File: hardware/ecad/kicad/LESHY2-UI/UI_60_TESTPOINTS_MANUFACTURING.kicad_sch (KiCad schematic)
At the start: 0 parts

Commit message: complete exact H2.2.10 UI test points
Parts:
- added TP1: TP_S3_RUN, TestPoint:TestPoint_Pad_D1.0mm, symbol Leshy2:UI60_TP_S3_RUN
- added TP10: TP_SLOW_IO_RESET_N, TestPoint:TestPoint_Pad_D1.0mm, symbol Leshy2:UI60_TP_SLOW_IO_RESET_N
- added TP11: TP_LCD_BACKLIGHT_FAULT_N, TestPoint:TestPoint_Pad_D1.0mm, symbol Leshy2:UI60_TP_LCD_BACKLIGHT_FAULT_N
- added TP2: TP_C5_RUN, TestPoint:TestPoint_Pad_D1.0mm, symbol Leshy2:UI60_TP_C5_RUN
- added TP3: TP_UI_TEMP, TestPoint:TestPoint_Pad_D1.0mm, symbol Leshy2:UI60_TP_UI_TEMP
- added TP4: TP_IR_TX_SAFE, TestPoint:TestPoint_Pad_D1.0mm, symbol Leshy2:UI60_TP_IR_TX_SAFE
- added TP5: TP_EV_N0, TestPoint:TestPoint_Pad_D1.0mm, symbol Leshy2:UI60_TP_EV_N0
- added TP6: TP_EV_N1, TestPoint:TestPoint_Pad_D1.0mm, symbol Leshy2:UI60_TP_EV_N1
- added TP7: TP_EV_N7, TestPoint:TestPoint_Pad_D1.0mm, symbol Leshy2:UI60_TP_EV_N7
- added TP8: TP_C5_SERVICE_VBUS_SENSE, TestPoint:TestPoint_Pad_D1.0mm, symbol Leshy2:UI60_TP_C5_SERVICE_VBUS_SENSE
- added TP9: TP_C5_GPIO27_FIXED_HIGH, TestPoint:TestPoint_Pad_D1.0mm, symbol Leshy2:UI60_TP_C5_GPIO27_FIXED_HIGH
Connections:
- new net C5_GPIO27_FIXED_HIGH: TP9.1 (TEST)
- new net C5_RESET_N: TP2.1 (TEST)
- new net C5_SERVICE_VBUS_SENSE_ONLY: TP8.1 (TEST)
- new net EV_N0_S3: TP5.1 (TEST)
- new net EV_N1_C5: TP6.1 (TEST)
- new net EV_N7_IR: TP7.1 (TEST)
- new net IR_TX_CARRIER_SAFE: TP4.1 (TEST)
- new net LCD_BACKLIGHT_FAULT_N: TP11.1 (TEST)
- new net S3_RESET_N: TP1.1 (TEST)
- new net SLOW_IO_RESET_N: TP10.1 (TEST)
- new net UI_ZONE_TEMP_ADC: TP3.1 (TEST)
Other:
- title: (none) -> Leshy2 — exact UI manufacturing and diagnostic test pads

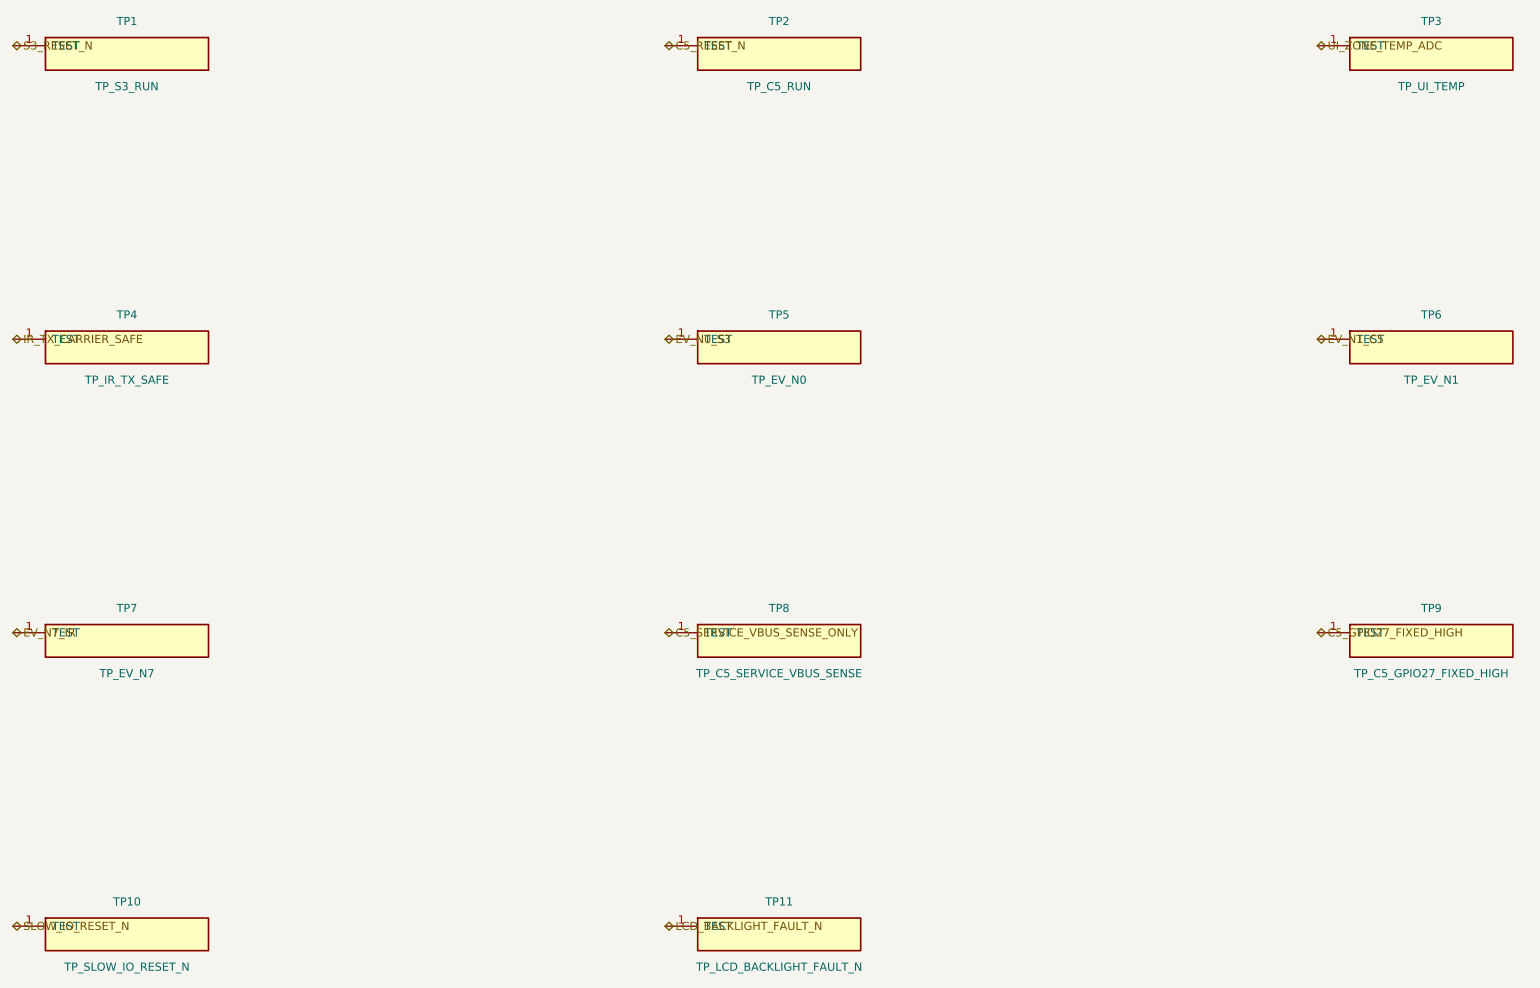
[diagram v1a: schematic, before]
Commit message: complete H2 schematic review package
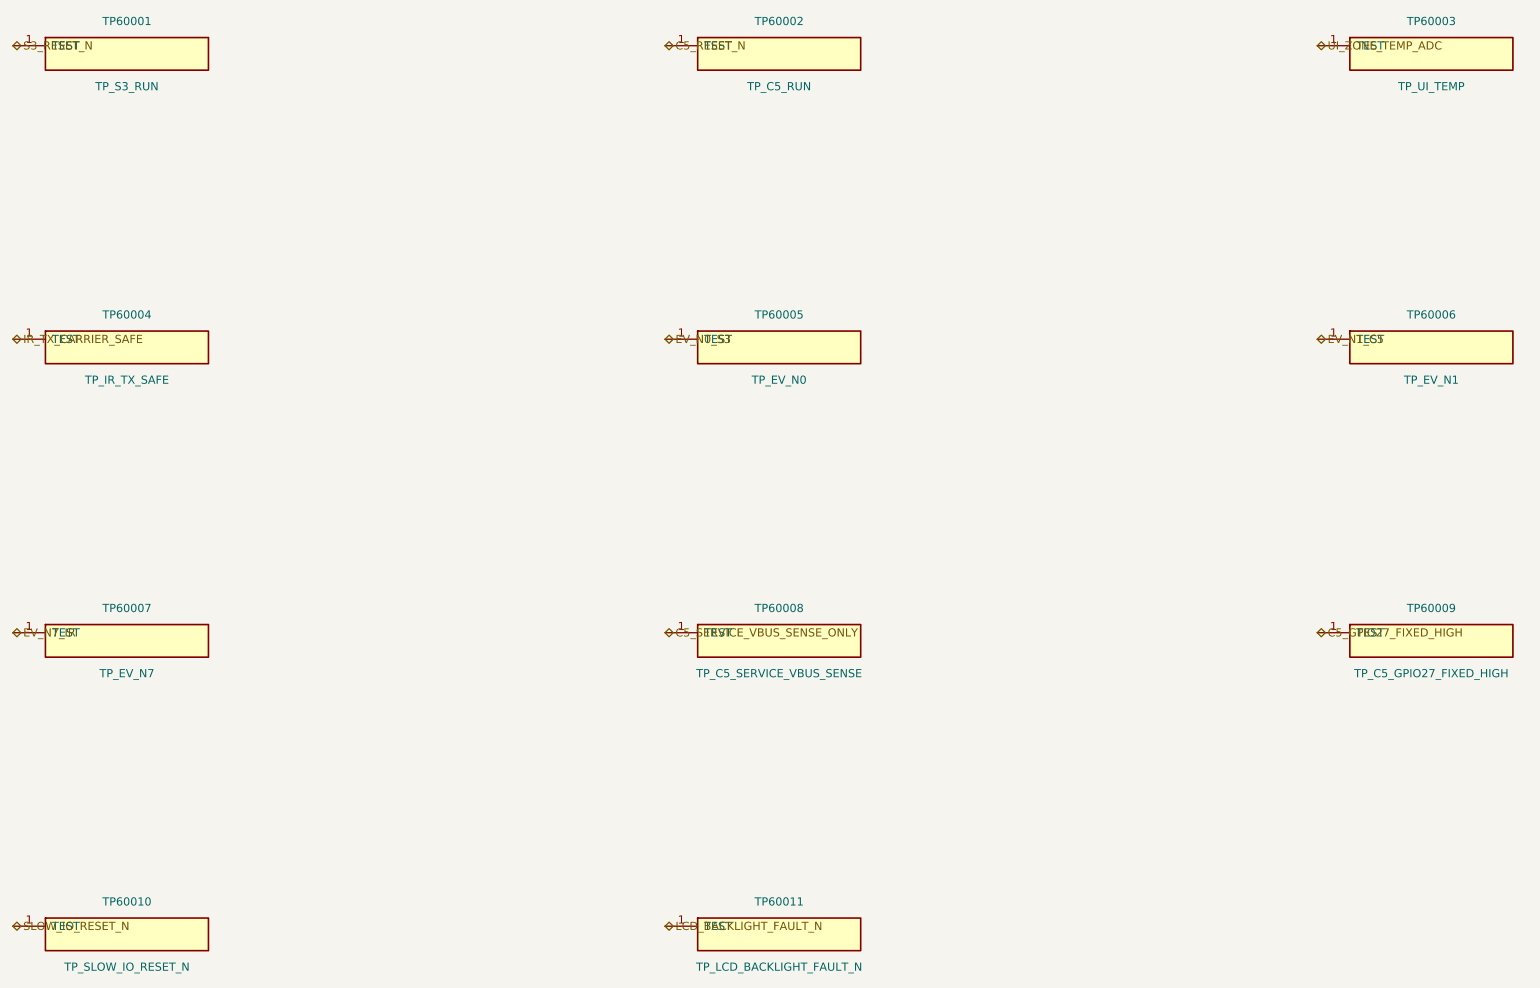
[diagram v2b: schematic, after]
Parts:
- renumbered TP1 to TP60001, TP2 to TP60002, TP3 to TP60003, TP4 to TP60004, TP5 to TP60005, TP6 to TP60006, TP7 to TP60007, TP8 to TP60008, TP9 to TP60009, TP10 to TP60010, TP11 to TP60011
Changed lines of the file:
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@@
 		(on_board yes)
 		(dnp no)
-		(property "Reference" "TP1"
+		(property "Reference" "TP60001"
 			(at 60.96 40.64 0)
 			(show_name no)
@@
 			(project "LESHY2-UI"
 				(path "/65f116c6-cf21-5e71-ad4e-c9698d9f768e"
-					(reference "TP1")
+					(reference "TP60001")
 					(unit 1)
 				)
@@
 		(on_board yes)
 		(dnp no)
-		(property "Reference" "TP2"
+		(property "Reference" "TP60002"
 			(at 162.56 40.64 0)
 			(show_name no)
@@
 			(project "LESHY2-UI"
 				(path "/65f116c6-cf21-5e71-ad4e-c9698d9f768e"
-					(reference "TP2")
+					(reference "TP60002")
 					(unit 1)
 				)
@@
 		(on_board yes)
 		(dnp no)
-		(property "Reference" "TP3"
+		(property "Reference" "TP60003"
 			(at 264.16 40.64 0)
 			(show_name no)
@@
 			(project "LESHY2-UI"
 				(path "/65f116c6-cf21-5e71-ad4e-c9698d9f768e"
-					(reference "TP3")
+					(reference "TP60003")
 					(unit 1)
 				)
@@
 		(on_board yes)
 		(dnp no)
-		(property "Reference" "TP4"
+		(property "Reference" "TP60004"
 			(at 60.96 86.36 0)
 			(show_name no)
@@
 			(project "LESHY2-UI"
 				(path "/65f116c6-cf21-5e71-ad4e-c9698d9f768e"
-					(reference "TP4")
+					(reference "TP60004")
 					(unit 1)
 				)
@@
 		(on_board yes)
 		(dnp no)
-		(property "Reference" "TP5"
+		(property "Reference" "TP60005"
 			(at 162.56 86.36 0)
 			(show_name no)
@@
 			(project "LESHY2-UI"
 				(path "/65f116c6-cf21-5e71-ad4e-c9698d9f768e"
-					(reference "TP5")
+					(reference "TP60005")
 					(unit 1)
 				)
@@
 		(on_board yes)
 		(dnp no)
-		(property "Reference" "TP6"
+		(property "Reference" "TP60006"
 			(at 264.16 86.36 0)
 			(show_name no)
@@
 			(project "LESHY2-UI"
 				(path "/65f116c6-cf21-5e71-ad4e-c9698d9f768e"
-					(reference "TP6")
+					(reference "TP60006")
 					(unit 1)
 				)
@@
 		(on_board yes)
 		(dnp no)
-		(property "Reference" "TP7"
+		(property "Reference" "TP60007"
 			(at 60.96 132.08 0)
 			(show_name no)
@@
 			(project "LESHY2-UI"
 				(path "/65f116c6-cf21-5e71-ad4e-c9698d9f768e"
-					(reference "TP7")
+					(reference "TP60007")
 					(unit 1)
 				)
@@
 		(on_board yes)
 		(dnp no)
-		(property "Reference" "TP8"
+		(property "Reference" "TP60008"
 			(at 162.56 132.08 0)
 			(show_name no)
@@
 			(project "LESHY2-UI"
 				(path "/65f116c6-cf21-5e71-ad4e-c9698d9f768e"
-					(reference "TP8")
+					(reference "TP60008")
 					(unit 1)
 				)
@@
 		(on_board yes)
 		(dnp no)
-		(property "Reference" "TP9"
+		(property "Reference" "TP60009"
 			(at 264.16 132.08 0)
 			(show_name no)
@@
 			(project "LESHY2-UI"
 				(path "/65f116c6-cf21-5e71-ad4e-c9698d9f768e"
-					(reference "TP9")
+					(reference "TP60009")
 					(unit 1)
 				)
@@
 		(on_board yes)
 		(dnp no)
-		(property "Reference" "TP10"
+		(property "Reference" "TP60010"
 			(at 60.96 177.80 0)
 			(show_name no)
@@
 			(project "LESHY2-UI"
 				(path "/65f116c6-cf21-5e71-ad4e-c9698d9f768e"
-					(reference "TP10")
+					(reference "TP60010")
 					(unit 1)
 				)
@@
 		(on_board yes)
 		(dnp no)
-		(property "Reference" "TP11"
+		(property "Reference" "TP60011"
 			(at 162.56 177.80 0)
 			(show_name no)
@@
 			(project "LESHY2-UI"
 				(path "/65f116c6-cf21-5e71-ad4e-c9698d9f768e"
-					(reference "TP11")
-					(unit 1)
-				)
+					(reference "TP60011")
+					(unit 1)
+				)
